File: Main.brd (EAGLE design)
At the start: 103.8 x 80 mm, 54 parts, among them IC1 LM75A, IC2 ADUM1400, IC3 74LS14N, Q1 IRF9530, U1 L298, U2 LM 1084 IT5,0, U3 LM 1084 IT3,3, U4 L298, X1 Motors, X3 Battery, X4 Ultra Sonics (5V), X5 ITG-3200, X6 PIRs

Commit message: optimizing board
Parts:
- X6: value PIRs -> PIRs (5V); device con-wago:233-506 -> con-wago:233-504
- moved X5 36.9 mm to (6.35, 50.8), turned to 180 degrees
- moved X6 25.2 mm to (63.5, 66.0)
- moved R2 22.2 mm to (25.4, 52.1)
- moved X4 21.3 mm to (43.2, 55.9), turned to 270 degrees
- moved R4 19.0 mm to (17.8, 53.3), turned to 90 degrees
- moved R5 18.2 mm to (21.6, 48.3)
- moved IC1 13.7 mm to (74.9, 55.9), turned to 270 degrees
- moved D7 12.7 mm to (2.54, 35.6)
- moved D4 12.5 mm to (19.1, 40.6), turned to 180 degrees
- moved F6 10.5 mm to (15.2, 5.08)
- moved IC3 7.73 mm to (76.2, 21.6)
- moved R3 7.73 mm to (26.7, 61.0), turned to 270 degrees
- moved F2 7.62 mm to (78.7, 76.2)
- moved R13 7.41 mm to (49.5, 27.9), turned to 90 degrees
- moved F3 6.84 mm to (8.89, 35.6)
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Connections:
- net +5V: no longer X6.B5
- net GND: no longer X6.B6
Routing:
- net GND: track 0.00 -> 546.0 mm, vias 0 -> 2
- net +12V: track 0.00 -> 285.7 mm, vias 0 -> 1
- net +5V: track 0.00 -> 207.8 mm, vias 0 -> 8
- net +3.3V: track 0.00 -> 140.9 mm, vias 0 -> 1
- net ML_OUT_A: track 0.00 -> 129.0 mm, vias 0 -> 5
- net MR_DIR: track 0.00 -> 108.3 mm, vias 0 -> 1
- net SDA1: track 0.00 -> 104.3 mm
- net SCL1: track 0.00 -> 104.1 mm, vias 0 -> 2
- net ML_OUT_B: track 0.00 -> 100.2 mm, vias 0 -> 1
- net MR_OUT_B: track 0.00 -> 98.0 mm
- net VCC: track 0.00 -> 93.8 mm
- net N$5: track 0.00 -> 79.7 mm, vias 0 -> 1
- net MR_OUT_A: track 0.00 -> 64.8 mm, vias 0 -> 2
- net ML_DIR: track 0.00 -> 59.7 mm
- net MR_B: track 0.00 -> 53.3 mm
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
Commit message: optimizing board
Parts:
- moved R5 15.5 mm to (36.8, 45.7), turned to 180 degrees
- moved R7 7.41 mm to (27.9, 63.5), turned to 180 degrees
- moved R4 6.84 mm to (20.3, 47.0), turned to 180 degrees
- moved X6 5.39 mm to (59.7, 69.8), turned to 0 degrees
- moved D2 4.02 mm to (21.6, 20.3), turned to 90 degrees
- moved X4 3.59 mm to (40.6, 58.4)
- moved IC2 2.84 mm to (64.8, 38.1)
- moved R2 2.84 mm to (24.1, 54.6)
- moved D3 2.54 mm to (19.1, 33.0), turned to 90 degrees
- moved D4 2.54 mm to (16.5, 40.6)
- moved R3 1.80 mm to (25.4, 59.7), turned to 180 degrees
- moved D11 1.27 mm to (29.2, 6.35)
- moved X5 1.27 mm to (7.62, 50.8)
- moved D10 1.27 mm to (27.9, 20.3), turned to 270 degrees
- moved D7 1.27 mm to (2.54, 36.8)
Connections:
- net PIR1: now also SV1.32; no longer SV1.40
- net PIR4: now also SV1.40; no longer SV1.32
- net SCL1: now also X5.B3; no longer X5.B4
- net SDA1: now also X5.B4; no longer X5.B3
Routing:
- net GND: track 546.0 -> 0.00 mm, vias 2 -> 0
- net +12V: track 285.7 -> 0.00 mm, vias 1 -> 0
- net +5V: track 207.8 -> 0.00 mm, vias 8 -> 0
- net +3.3V: track 140.9 -> 0.00 mm, vias 1 -> 0
- net ML_OUT_A: track 129.0 -> 0.00 mm, vias 5 -> 0
- net MR_DIR: track 108.3 -> 0.00 mm, vias 1 -> 0
- net SDA1: track 104.3 -> 0.00 mm
- net SCL1: track 104.1 -> 0.00 mm, vias 2 -> 0
- net ML_OUT_B: track 100.2 -> 0.00 mm, vias 1 -> 0
- net MR_OUT_B: track 98.0 -> 0.00 mm
- net VCC: track 93.8 -> 0.00 mm
- net N$5: track 79.7 -> 0.00 mm, vias 1 -> 0
- net MR_OUT_A: track 64.8 -> 0.00 mm, vias 2 -> 0
- net ML_DIR: track 59.7 -> 0.00 mm
- net MR_B: track 53.3 -> 0.00 mm
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
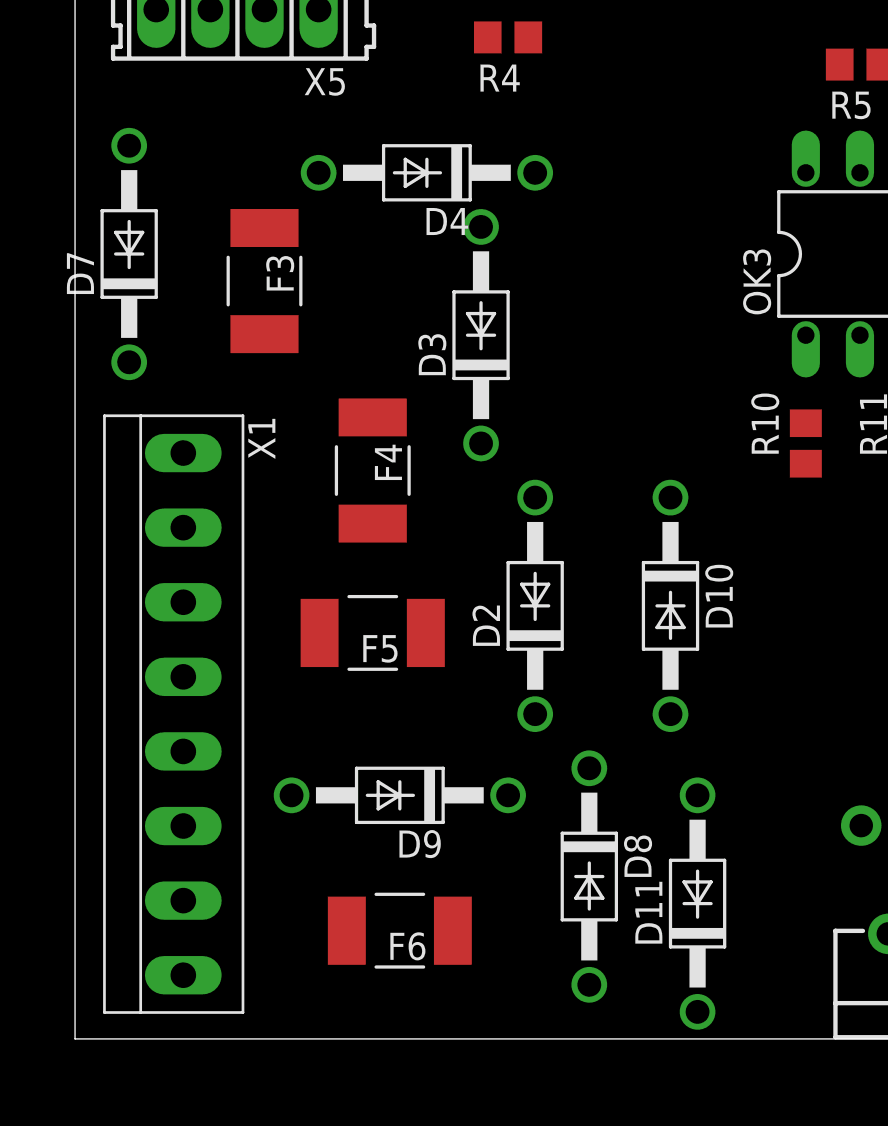
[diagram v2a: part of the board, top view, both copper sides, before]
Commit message: smd protection diodes for h bridge
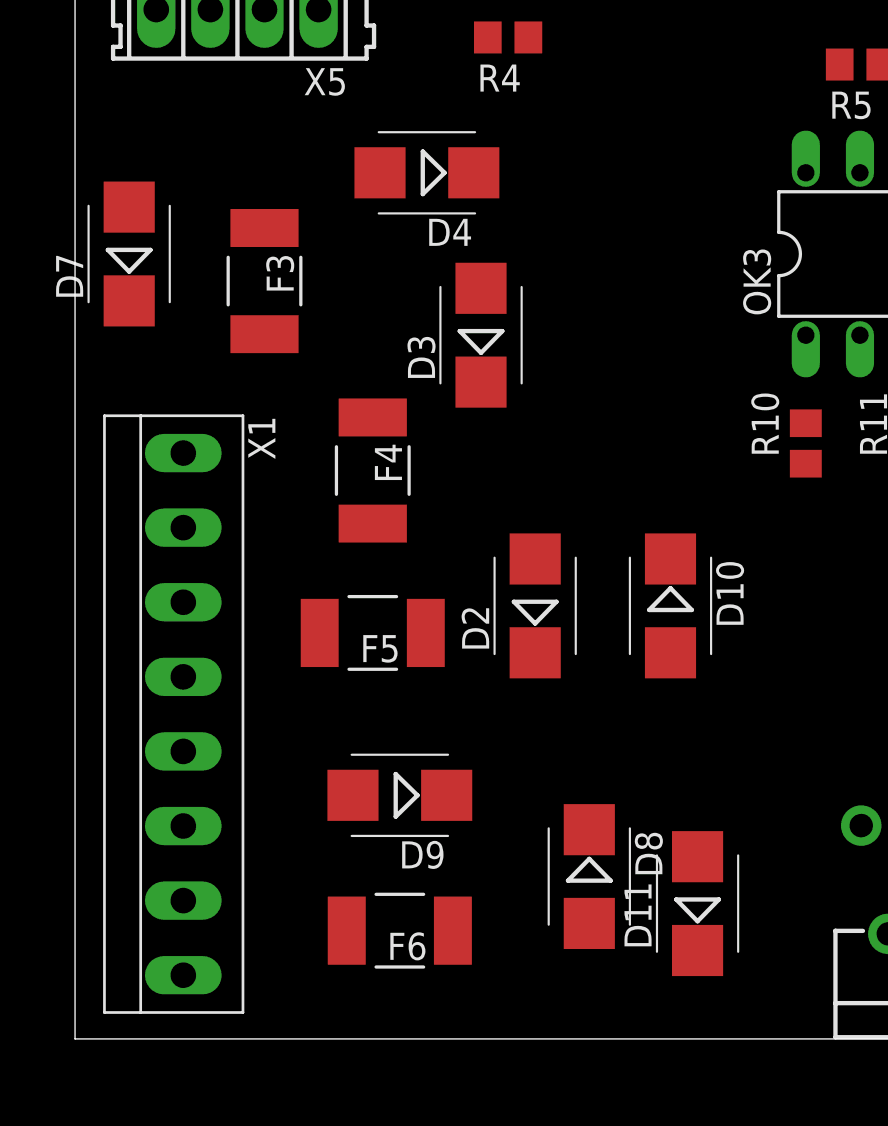
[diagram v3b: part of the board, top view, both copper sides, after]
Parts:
- D10, D11, D2, D3, D4, D7, D8, D9: value UF4003 -> ES 2BA; device diode:DO41-10 -> diode:SMB
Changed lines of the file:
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@@
 <element name="C7" library="rcl" package="C0805" value="100nF" x="95.25" y="62.23"/>
 <element name="C8" library="rcl" package="C0805" value="100nF" x="90.17" y="53.34"/>
-<element name="D10" library="diode" package="DO41-10" value="UF4003" x="27.94" y="20.32" rot="R270"/>
-<element name="D11" library="diode" package="DO41-10" value="UF4003" x="29.21" y="6.35" rot="R90"/>
-<element name="D2" library="diode" package="DO41-10" value="UF4003" x="21.59" y="20.32" rot="R90"/>
-<element name="D3" library="diode" package="DO41-10" value="UF4003" x="19.05" y="33.02" rot="R90"/>
-<element name="D4" library="diode" package="DO41-10" value="UF4003" x="16.51" y="40.64" rot="R180"/>
-<element name="D7" library="diode" package="DO41-10" value="UF4003" x="2.54" y="36.83" rot="R90"/>
-<element name="D8" library="diode" package="DO41-10" value="UF4003" x="24.13" y="7.62" rot="R270"/>
-<element name="D9" library="diode" package="DO41-10" value="UF4003" x="15.24" y="11.43" rot="R180"/>
+<element name="D10" library="diode" package="SMB" value="ES 2BA" x="27.94" y="20.32" rot="R270"/>
+<element name="D11" library="diode" package="SMB" value="ES 2BA" x="29.21" y="6.35" rot="R90"/>
+<element name="D2" library="diode" package="SMB" value="ES 2BA" x="21.59" y="20.32" rot="R90"/>
+<element name="D3" library="diode" package="SMB" value="ES 2BA" x="19.05" y="33.02" rot="R90"/>
+<element name="D4" library="diode" package="SMB" value="ES 2BA" x="16.51" y="40.64" rot="R180"/>
+<element name="D7" library="diode" package="SMB" value="ES 2BA" x="2.54" y="36.83" rot="R90"/>
+<element name="D8" library="diode" package="SMB" value="ES 2BA" x="24.13" y="7.62" rot="R270"/>
+<element name="D9" library="diode" package="SMB" value="ES 2BA" x="15.24" y="11.43" rot="R180"/>
 <element name="SV1" library="con-lsta" package="FE20-2" value="Raspberry Pi B Plus Connector" x="26.67" y="72.39" rot="MR180">
 <attribute name="OC_NEWARK" value="unknown" x="26.67" y="72.39" size="1.778" layer="28" rot="MR180" display="off"/>
@@
 <wire x1="72.45" y1="4.93" x2="81.11" y2="3.81" width="0" layer="19" extent="1-1"/>
 <wire x1="50.86" y1="4.93" x2="72.45" y2="4.93" width="0" layer="19" extent="1-1"/>
-<wire x1="24.13" y1="12.7" x2="50.86" y2="4.93" width="0" layer="19" extent="1-1"/>
-<wire x1="21.59" y1="15.24" x2="24.13" y2="12.7" width="0" layer="19" extent="1-1"/>
-<wire x1="20.32" y1="11.43" x2="24.13" y2="12.7" width="0" layer="19" extent="1-1"/>
-<wire x1="19.05" y1="27.94" x2="21.59" y2="15.24" width="0" layer="19" extent="1-1"/>
+<wire x1="24.13" y1="9.82" x2="50.86" y2="4.93" width="0" layer="19" extent="1-1"/>
+<wire x1="17.44" y1="11.43" x2="24.13" y2="9.82" width="0" layer="19" extent="1-1"/>
+<wire x1="21.59" y1="18.12" x2="17.44" y2="11.43" width="0" layer="19" extent="1-1"/>
+<wire x1="19.05" y1="30.82" x2="21.59" y2="18.12" width="0" layer="19" extent="1-1"/>
 </signal>
 <signal name="GND" class="1">
@@
 <wire x1="60.325" y1="42.7" x2="67.945" y2="42.7" width="0" layer="19" extent="1-1"/>
 <wire x1="72.33" y1="53.975" x2="67.945" y2="42.7" width="0" layer="19" extent="1-1"/>
-<wire x1="27.94" y1="15.24" x2="36.83" y2="33.02" width="0" layer="19" extent="1-1"/>
-<wire x1="29.21" y1="11.43" x2="27.94" y2="15.24" width="0" layer="19" extent="1-1"/>
-<wire x1="45.78" y1="4.93" x2="29.21" y2="11.43" width="0" layer="19" extent="1-1"/>
+<wire x1="27.94" y1="18.12" x2="36.83" y2="33.02" width="0" layer="19" extent="1-1"/>
+<wire x1="29.21" y1="8.55" x2="27.94" y2="18.12" width="0" layer="19" extent="1-1"/>
+<wire x1="45.78" y1="4.93" x2="29.21" y2="8.55" width="0" layer="19" extent="1-1"/>
 <wire x1="67.37" y1="4.93" x2="68.58" y2="25.4" width="0" layer="19" extent="1-1"/>
 <wire x1="19.37" y1="46.99" x2="36.83" y2="33.02" width="0" layer="19" extent="1-1"/>
+<wire x1="14.31" y1="40.64" x2="19.37" y2="46.99" width="0" layer="19" extent="1-1"/>
 <wire x1="24.13" y1="53.66" x2="19.37" y2="46.99" width="0" layer="19" extent="1-1"/>
-<wire x1="11.43" y1="40.64" x2="19.37" y2="46.99" width="0" layer="19" extent="1-1"/>
-<wire x1="2.54" y1="41.91" x2="11.43" y2="40.64" width="0" layer="19" extent="1-1"/>
+<wire x1="2.54" y1="39.03" x2="14.31" y2="40.64" width="0" layer="19" extent="1-1"/>
 <wire x1="8.89" y1="53.3" x2="19.37" y2="46.99" width="0" layer="19" extent="1-1"/>
 <wire x1="11.43" y1="62.55" x2="8.89" y2="53.3" width="0" layer="19" extent="1-1"/>
@@
 <contactref element="X1" pad="4"/>
 <wire x1="61.02" y1="10.01" x2="73.72" y2="10.01" width="0" layer="19" extent="1-1"/>
-<wire x1="21.59" y1="40.64" x2="61.02" y2="10.01" width="0" layer="19" extent="1-1"/>
-<wire x1="19.05" y1="38.1" x2="21.59" y2="40.64" width="0" layer="19" extent="1-1"/>
-<wire x1="5.08" y1="23.99" x2="19.05" y2="38.1" width="0" layer="19" extent="1-1"/>
+<wire x1="19.05" y1="35.22" x2="61.02" y2="10.01" width="0" layer="19" extent="1-1"/>
+<wire x1="18.71" y1="40.64" x2="19.05" y2="35.22" width="0" layer="19" extent="1-1"/>
+<wire x1="5.08" y1="23.99" x2="19.05" y2="35.22" width="0" layer="19" extent="1-1"/>
 <wire x1="5.08" y1="16.99" x2="5.08" y2="23.99" width="0" layer="19" extent="1-1"/>
 </signal>
@@
 <contactref element="F4" pad="1"/>
 <wire x1="59.75" y1="4.93" x2="74.99" y2="4.93" width="0" layer="19" extent="1-1"/>
-<wire x1="21.59" y1="25.4" x2="59.75" y2="4.93" width="0" layer="19" extent="1-1"/>
-<wire x1="13.97" y1="29.16" x2="21.59" y2="25.4" width="0" layer="19" extent="1-1"/>
+<wire x1="21.59" y1="22.52" x2="59.75" y2="4.93" width="0" layer="19" extent="1-1"/>
+<wire x1="13.97" y1="29.16" x2="21.59" y2="22.52" width="0" layer="19" extent="1-1"/>
 <wire x1="8.89" y1="38.05" x2="13.97" y2="29.16" width="0" layer="19" extent="1-1"/>
-<wire x1="2.54" y1="31.75" x2="8.89" y2="38.05" width="0" layer="19" extent="1-1"/>
+<wire x1="2.54" y1="34.63" x2="8.89" y2="38.05" width="0" layer="19" extent="1-1"/>
 </signal>
 <signal name="MR_B">
@@
 <contactref element="F6" pad="1"/>
 <wire x1="38.16" y1="4.93" x2="53.4" y2="4.93" width="0" layer="19" extent="1-1"/>
-<wire x1="29.21" y1="1.27" x2="38.16" y2="4.93" width="0" layer="19" extent="1-1"/>
-<wire x1="24.13" y1="2.54" x2="29.21" y2="1.27" width="0" layer="19" extent="1-1"/>
-<wire x1="17.73" y1="5.08" x2="24.13" y2="2.54" width="0" layer="19" extent="1-1"/>
+<wire x1="29.21" y1="4.15" x2="38.16" y2="4.93" width="0" layer="19" extent="1-1"/>
+<wire x1="24.13" y1="5.42" x2="29.21" y2="4.15" width="0" layer="19" extent="1-1"/>
+<wire x1="17.73" y1="5.08" x2="24.13" y2="5.42" width="0" layer="19" extent="1-1"/>
 <wire x1="16.46" y1="19.05" x2="17.73" y2="5.08" width="0" layer="19" extent="1-1"/>
 </signal>
@@
 <contactref element="X1" pad="8"/>
 <wire x1="39.43" y1="10.01" x2="52.13" y2="10.01" width="0" layer="19" extent="1-1"/>
-<wire x1="27.94" y1="25.4" x2="39.43" y2="10.01" width="0" layer="19" extent="1-1"/>
-<wire x1="10.16" y1="11.43" x2="27.94" y2="25.4" width="0" layer="19" extent="1-1"/>
-<wire x1="5.08" y1="9.99" x2="10.16" y2="11.43" width="0" layer="19" extent="1-1"/>
+<wire x1="27.94" y1="22.52" x2="39.43" y2="10.01" width="0" layer="19" extent="1-1"/>
+<wire x1="13.04" y1="11.43" x2="27.94" y2="22.52" width="0" layer="19" extent="1-1"/>
+<wire x1="5.08" y1="9.99" x2="13.04" y2="11.43" width="0" layer="19" extent="1-1"/>
 <wire x1="5.08" y1="2.99" x2="5.08" y2="9.99" width="0" layer="19" extent="1-1"/>
 </signal>

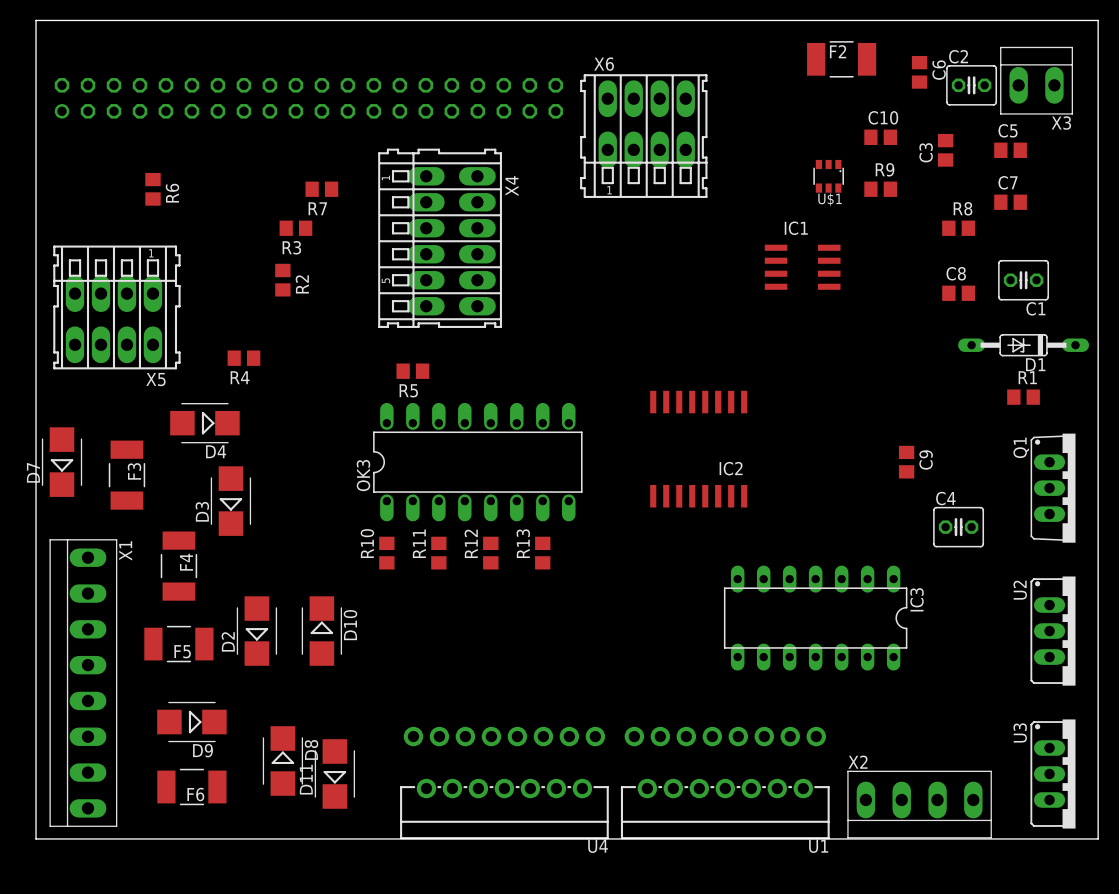
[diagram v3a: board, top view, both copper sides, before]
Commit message: gpio expander
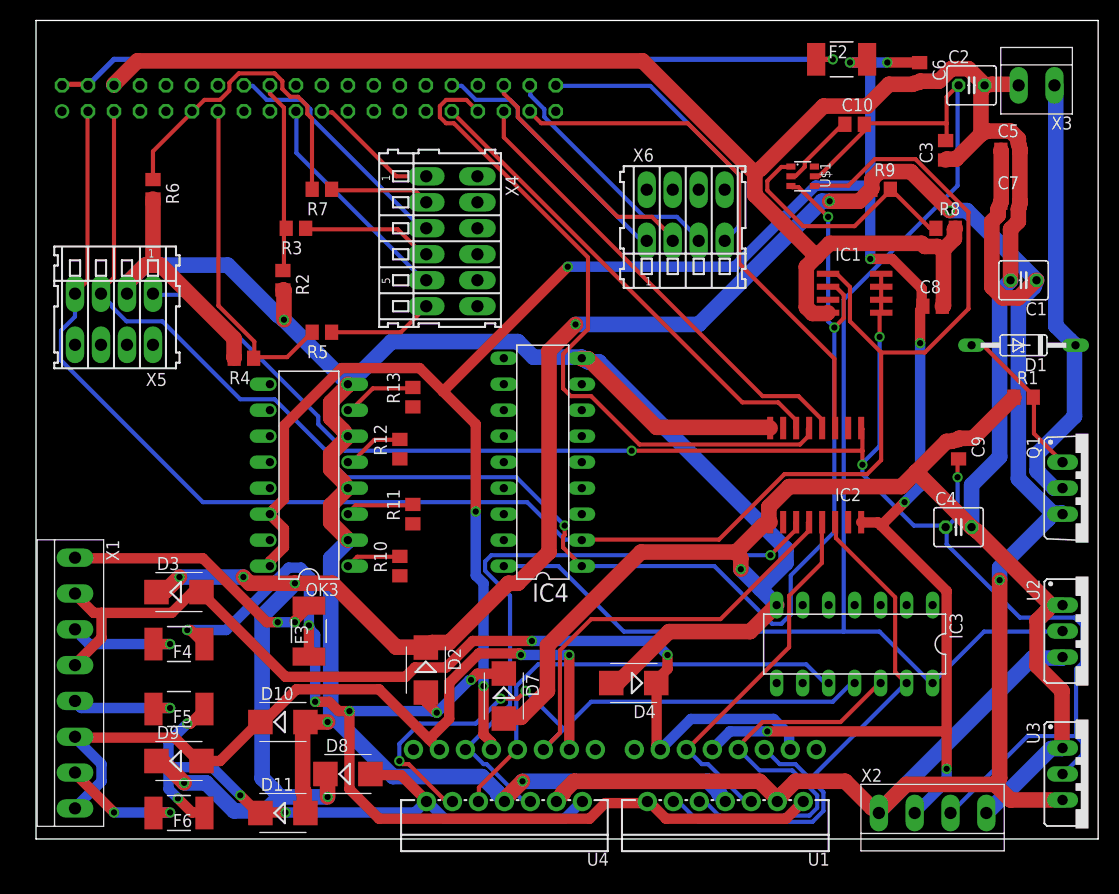
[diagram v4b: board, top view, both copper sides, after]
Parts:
- added IC4: MCP2300X/P, adafruit:DIL18
- moved D4 49.0 mm to (58.4, 15.2)
- moved D7 48.9 mm to (45.7, 14.0), turned to 270 degrees
- moved F3 23.4 mm to (26.7, 20.3), turned to 90 degrees
- moved R13 19.8 mm to (36.8, 43.2)
- moved D2 16.9 mm to (38.1, 16.5), turned to 270 degrees
- moved OK3 16.6 mm to (26.7, 35.6), turned to 90 degrees
- moved R12 13.5 mm to (35.6, 38.1)
- moved IC2 11.7 mm to (76.2, 35.6)
- moved D3 10.2 mm to (14.0, 24.1), turned to 0 degrees
- moved D10 9.67 mm to (24.1, 11.4), turned to 0 degrees
- moved R5 9.67 mm to (27.9, 49.5)
- moved X6 9.67 mm to (63.5, 61.0)
- moved F4 7.62 mm to (14.0, 19.1), turned to 180 degrees
- moved D8 6.48 mm to (30.5, 6.35), turned to 0 degrees
- moved D11 6.35 mm to (24.1, 2.54), turned to 0 degrees
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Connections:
- net N$1 renamed ML_DIR_
- net N$12 renamed MR_SPEED_
- net N$6 renamed ML_SPEED_
- net N$8 renamed MR_DIR_
- new net CAM_SERVO_AZI: OK3.15
- new net CAM_SERVO_ELE: OK3.13
- new net N$1: IC4.10
- new net N$12: IC4.13
- new net N$27: IC4.14
- new net N$28: IC4.15
- new net N$29: IC4.16
- new net N$31: IC4.17
- new net N$35: IC4.6
- new net N$37: IC4.8
- new net N$40: IC4.5
- new net N$41: IC4.4
- new net N$42: IC4.3
- new net N$6: IC4.11
- new net N$8: IC4.12
- net GND: now also IC4.9
- net SCL1: now also IC4.1
- net SDA1: now also IC4.2
- net VCC: now also IC4.18
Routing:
- net GND: track 0.00 -> 557.1 mm, vias 0 -> 4
- net +12V: track 0.00 -> 323.5 mm, vias 0 -> 9
- net +5V: track 0.00 -> 238.0 mm, vias 0 -> 10
- net SDA1: track 0.00 -> 175.1 mm
- net +3.3V: track 0.00 -> 167.3 mm, vias 0 -> 4
- net SCL1: track 0.00 -> 152.7 mm, vias 0 -> 3
- net VCC: track 0.00 -> 140.9 mm
- net ML_OUT_A: track 0.00 -> 110.8 mm, vias 0 -> 6
- net MR_DIR: track 0.00 -> 101.9 mm, vias 0 -> 3
- net ML_OUT_B: track 0.00 -> 97.1 mm, vias 0 -> 2
- net MR_OUT_B: track 0.00 -> 79.6 mm, vias 0 -> 2
- net N$5: track 0.00 -> 78.1 mm, vias 0 -> 1
- net MR_DIR_: track 0.00 -> 66.9 mm
- net MR_OUT_A: track 0.00 -> 64.7 mm, vias 0 -> 4
- net MR_SPEED: track 0.00 -> 62.2 mm, vias 0 -> 1
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
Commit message: 100% route
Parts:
- moved IC2 17.6 mm to (85.1, 20.3)
- moved R12 11.4 mm to (45.7, 33.0), turned to 180 degrees
- moved R13 10.9 mm to (45.7, 36.8), turned to 180 degrees
- moved IC3 10.9 mm to (69.8, 22.9), turned to 90 degrees
- moved R10 10.2 mm to (45.7, 26.7), turned to 180 degrees
- moved R11 8.98 mm to (45.7, 30.5), turned to 180 degrees
- moved D4 8.52 mm to (50.8, 19.1), turned to 0 degrees
- moved OK3 7.73 mm to (34.3, 34.3)
- moved IC4 7.73 mm to (57.1, 35.6)
- moved C4 4.02 mm to (94.0, 31.8), turned to 90 degrees
- moved F3 3.81 mm to (22.9, 20.3)
- moved D2 1.80 mm to (36.8, 15.2)
- moved C9 1.80 mm to (88.9, 39.4)
- moved U1 1.27 mm to (68.6, 6.35)
- turned D7 to 180 degrees
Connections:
- net N$1 renamed GP0
- net N$12 renamed GP3
- net N$6 renamed GP1
- net N$8 renamed GP2
- removed net N$27: IC4.14
- removed net N$28: IC4.15
- removed net N$29: IC4.16
- removed net N$31: IC4.17
- new net GP4: IC4.14, R13.1
- new net GP5: IC4.15, R12.1
- new net GP6: IC4.16, R11.1
- new net GP7: IC4.17, R10.1
- net GND: now also IC2.3
- net ML_DIR_: no longer IC2.3
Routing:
- net +5V: track 238.0 -> 175.3 mm, vias 10 -> 8
- net +12V: track 323.5 -> 266.7 mm, vias 9 -> 7
- net ML_DIR_: track 51.7 -> 0.00 mm
- net MR_DIR: track 101.9 -> 55.1 mm, vias 3 -> 2
- net ML_OUT_A: track 110.8 -> 77.0 mm
- net MR_SPEED_: track 46.9 -> 74.9 mm
- net GND: track 557.1 -> 529.6 mm
- net SDA1: track 175.1 -> 151.2 mm, vias 0 -> 2
- net +3.3V: track 167.3 -> 146.2 mm, vias 4 -> 1
- net ML_B: track 40.0 -> 19.9 mm
- net MR_OUT_B: track 79.6 -> 61.6 mm, vias 2 -> 0
- net ML_SPEED_: track 45.9 -> 62.8 mm
- net MR_B: track 45.1 -> 32.6 mm
- net SCL1: track 152.7 -> 140.3 mm, vias 3 -> 2
- net ML_DIR: track 57.2 -> 65.4 mm, vias 0 -> 1
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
